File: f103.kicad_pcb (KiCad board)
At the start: 2 copper layers, 337.2 x 122.6 mm, 213 parts, among them J1 Conn_01x01_Female, J2 Conn_01x01_Female, J3 Conn_01x01_Female, J4 Conn_01x01_Female, Q1 2N7002, SW1 Rotary_Encoder_Switch, U1 STM32F103CBTx, U2 XC6206P332MR, U3 SRV05-4, Y1 8MHz

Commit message: Finalizing
- Firmware creation begun
- add .step model of PCB
- add gerbers, CPL, BOM
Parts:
- SW1: footprint Rotary_Encoder:RotaryEncoder_Alps_EC11E-Switch_Vertical_H20mm -> edits:RotaryEncoder_Alps_EC11E-Switch_Vertical_H20mm
- moved R70 0.28 mm to (143.7, 80.4)
- moved R71 0.18 mm to (146.5, 79.3)
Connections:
- net ENCA renamed EA
- net ENCB renamed EB
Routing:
- net GND: track 140.2 -> 135.2 mm
- net R1: track 280.2 -> 279.3 mm
- net +5V: track 1752.4 -> 1751.7 mm
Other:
- board text added: "+"
- board text added: "-"

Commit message: mx
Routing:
- net D-: track 104.3 -> 110.1 mm
- net D+: track 104.7 -> 110.0 mm
- net EA: track 174.5 -> 176.3 mm
- net EB: track 170.4 -> 171.8 mm

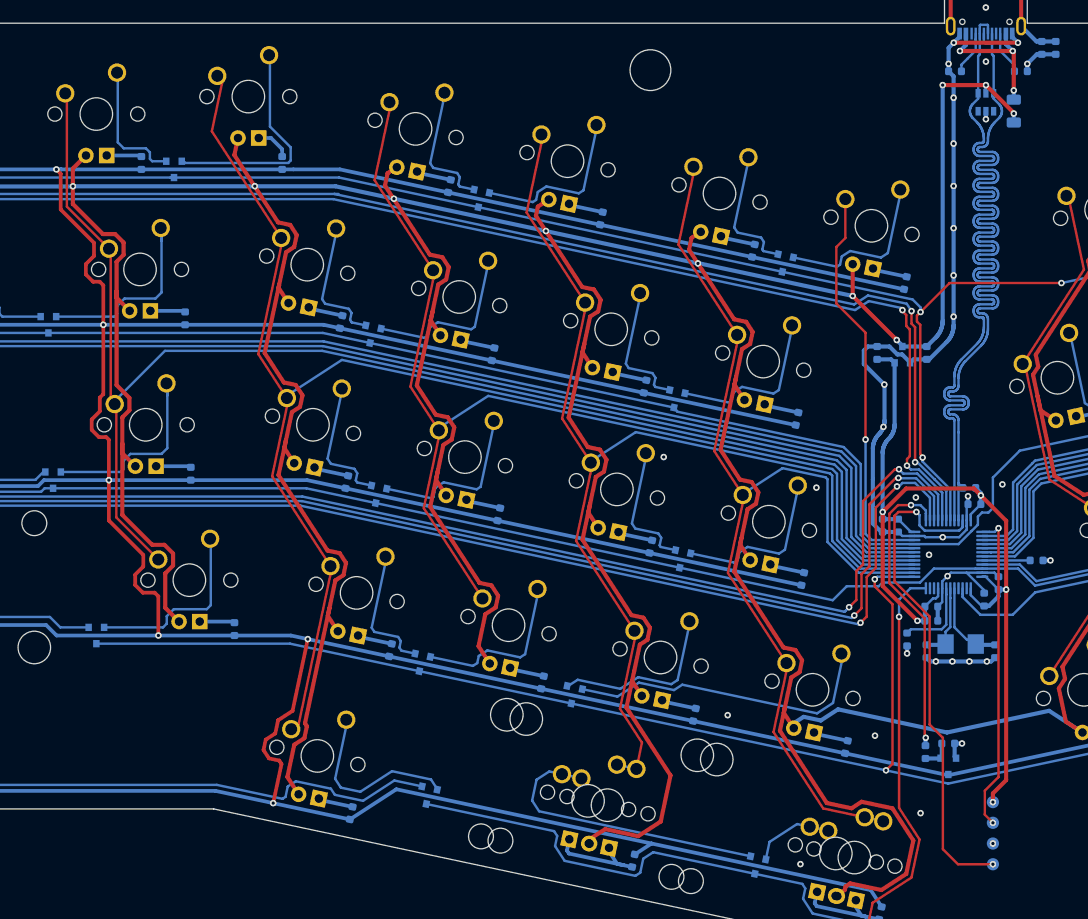
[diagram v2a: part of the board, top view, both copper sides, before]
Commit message: overhaul: see description
- remapped backlighting to A9
- remapped encoder pad B to B12
- updated ground fills
- added 02 silkscreen
- write firmware
- add compiled binary file
- begin acrylic case
- update gerbers and component placement files
- update readme images
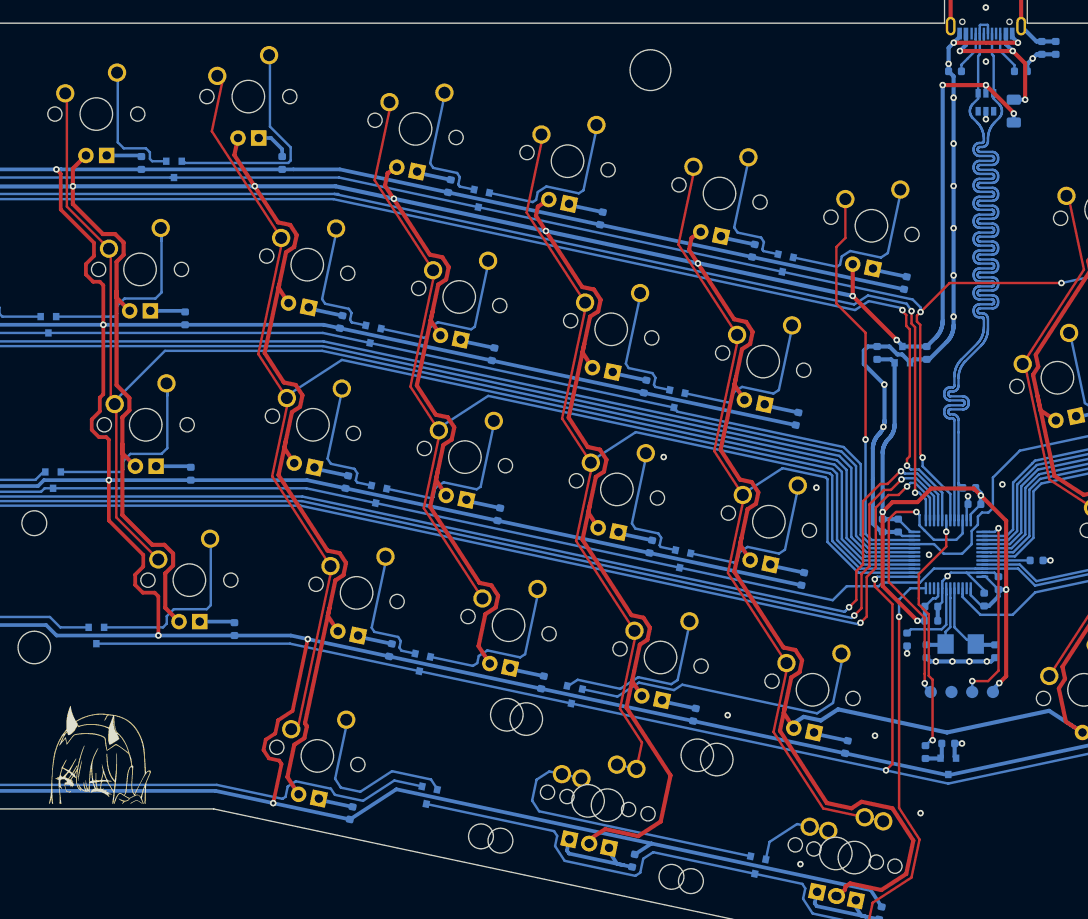
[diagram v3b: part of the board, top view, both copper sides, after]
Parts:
- added G2: zero, Graphics:02, F.Cu at (42.5, 80.3)
- added G3: zero, Graphics:02, B.Cu at (41.9, 80.3)
- moved J1 22.5 mm to (144.4, 73.0)
- moved J2 19.3 mm to (146.9, 73.0)
- moved J3 16.2 mm to (149.5, 73.0)
- moved J4 13.5 mm to (152.0, 73.0)
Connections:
- U1 pad 25: LED_PWM -> EB
- U1 pad 30: EB -> LED_PWM
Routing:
- net SWDIO: track 61.5 -> 36.9 mm
- net SWCLK: track 39.4 -> 24.7 mm
- net VBAT: track 115.3 -> 101.8 mm
- net GND: track 135.2 -> 127.2 mm, vias 45 -> 42
- net LED_PWM: track 36.7 -> 30.2 mm
- net VBUS: track 17.4 -> 19.4 mm
- net R1: track 279.3 -> 281.3 mm
- net EB: track 171.8 -> 170.9 mm

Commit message: ordered prototypes
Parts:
- G2, G3: footprint Graphics:02 -> Graphics:0222
- moved G3 3.18 mm to (41.8, 77.1)
- moved G2 3.17 mm to (42.5, 77.1)
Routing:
- net +5V: track 1751.7 -> 1758.9 mm
- net R1: track 281.3 -> 279.3 mm
- net D+: track 110.0 -> 110.9 mm
- net R4: track 214.5 -> 213.7 mm
- net GND: vias 42 -> 40
